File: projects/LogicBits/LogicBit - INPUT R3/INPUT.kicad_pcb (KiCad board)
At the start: 2 copper layers, 15.2 x 25.4 mm, 8 parts, among them P2 JMP_IN, P6 JMP_OUT, SW1 SWITCH_INV

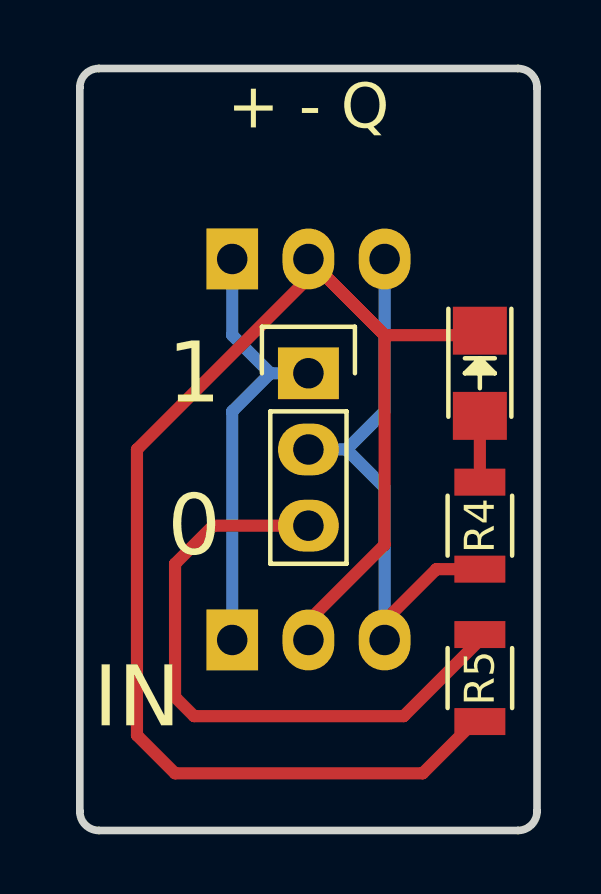
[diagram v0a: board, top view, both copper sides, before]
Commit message: Logic bit updates to input and bit.
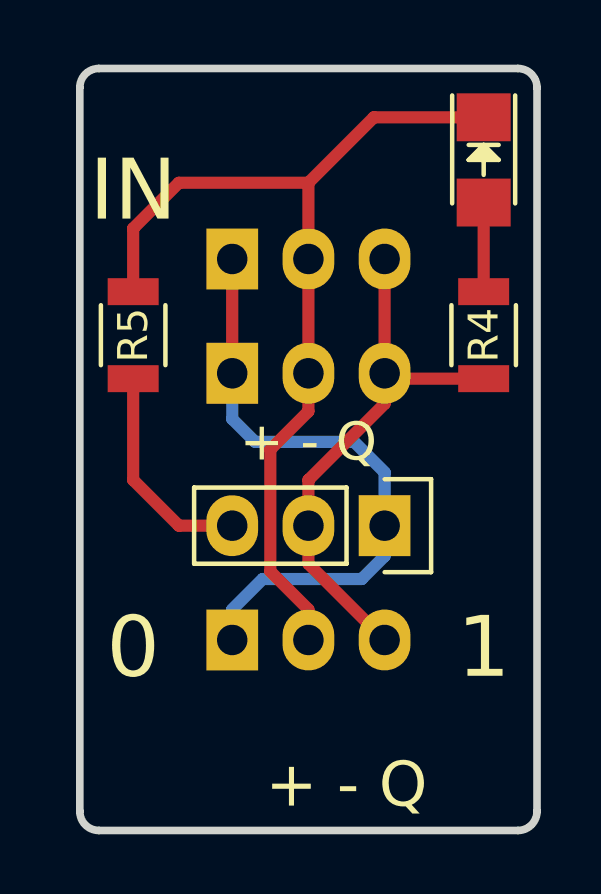
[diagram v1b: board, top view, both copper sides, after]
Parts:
- added P1: JMP_OUT, Pin_Headers:Pin_Header_Straight_1x03, F.Cu at (137.2, 94.0)
- R5: value 100K330 -> 1K
- moved R5 16.3 mm to (133.9, 92.7), turned to 90 degrees
- moved VAL 10.8 mm to (140.0, 106.4), turned to 0 degrees
- moved D1 7.11 mm to (145.5, 86.9)
- moved R4 6.35 mm to (145.5, 92.7)
- moved SW1 5.68 mm to (142.2, 99.1), turned to 270 degrees
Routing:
- net GND: track 52.5 -> 31.6 mm
- net Net-(R5-Pad1): track 21.1 -> 7.31 mm
- net +5V: track 15.0 -> 20.8 mm
- net Net-(P1-Pad3): track 19.5 -> 18.2 mm
- net Net-(D1-Pad2): track 2.21 -> 2.97 mm
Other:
- board text added: "Rev. 0.4"
- board text removed: "Rev. 0.3"
